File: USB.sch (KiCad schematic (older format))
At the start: 41 parts, among them J6 USB_A, J7 USB_B, U10 USB3320, U11 MIC2025-1YMM, U12 USB3320, U20 xc7z020clg484, Y1 ABM3-24.000MHZ-D2Y-T, Y2 ABM3-24.000MHZ-D2Y-T

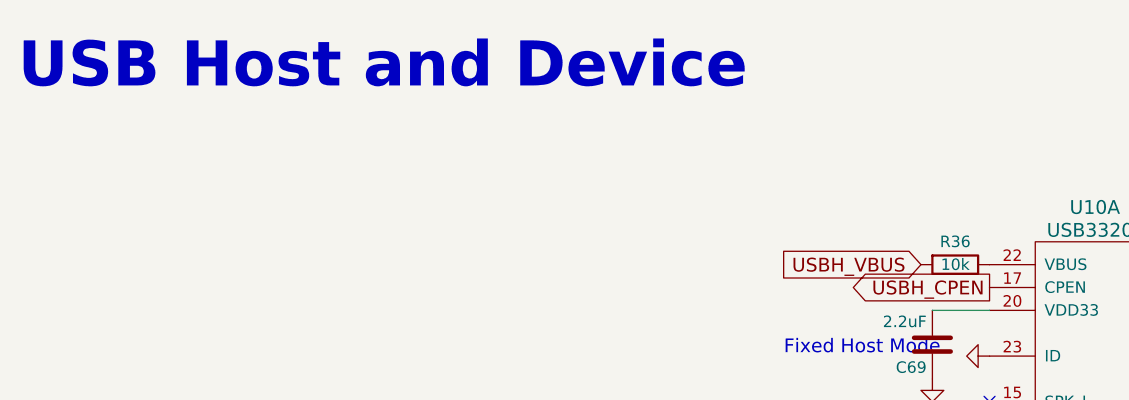
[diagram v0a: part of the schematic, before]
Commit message: low 2 ddr3 bytes delay matched WRT package flight time
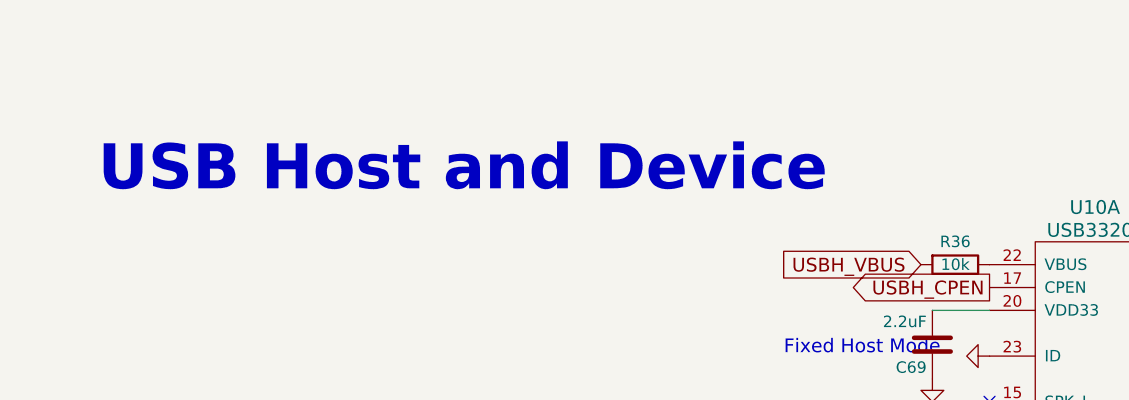
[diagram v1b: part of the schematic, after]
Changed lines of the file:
@@
 	1    0    0    -1
 $EndComp
-Text Notes 250  550  0    197  ~ 39
+Text Notes 600  1000 0    197  ~ 39
 USB Host and Device
 $EndSCHEMATC

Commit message: added arduino header, shifted components, deleted 50pin ZIF, deleted MIDI in for fear of confusion with headphone jack
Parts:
- J7: footprint Connector_USB:USB_B_Amphenol_MUSB-D511_Vertical_Rugged -> Connector_USB:USB_B_OST_USB-B1HSxx_Horizontal
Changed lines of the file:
@@
 F 0 "J7" H 9305 5367 50  0000 C CNN
 F 1 "USB_B" H 9305 5276 50  0000 C CNN
-F 2 "Connector_USB:USB_B_Amphenol_MUSB-D511_Vertical_Rugged" H 9400 4850 50  0001 C CNN
+F 2 "Connector_USB:USB_B_OST_USB-B1HSxx_Horizontal" H 9400 4850 50  0001 C CNN
 F 3 " ~" H 9400 4850 50  0001 C CNN
 	1    9250 4900

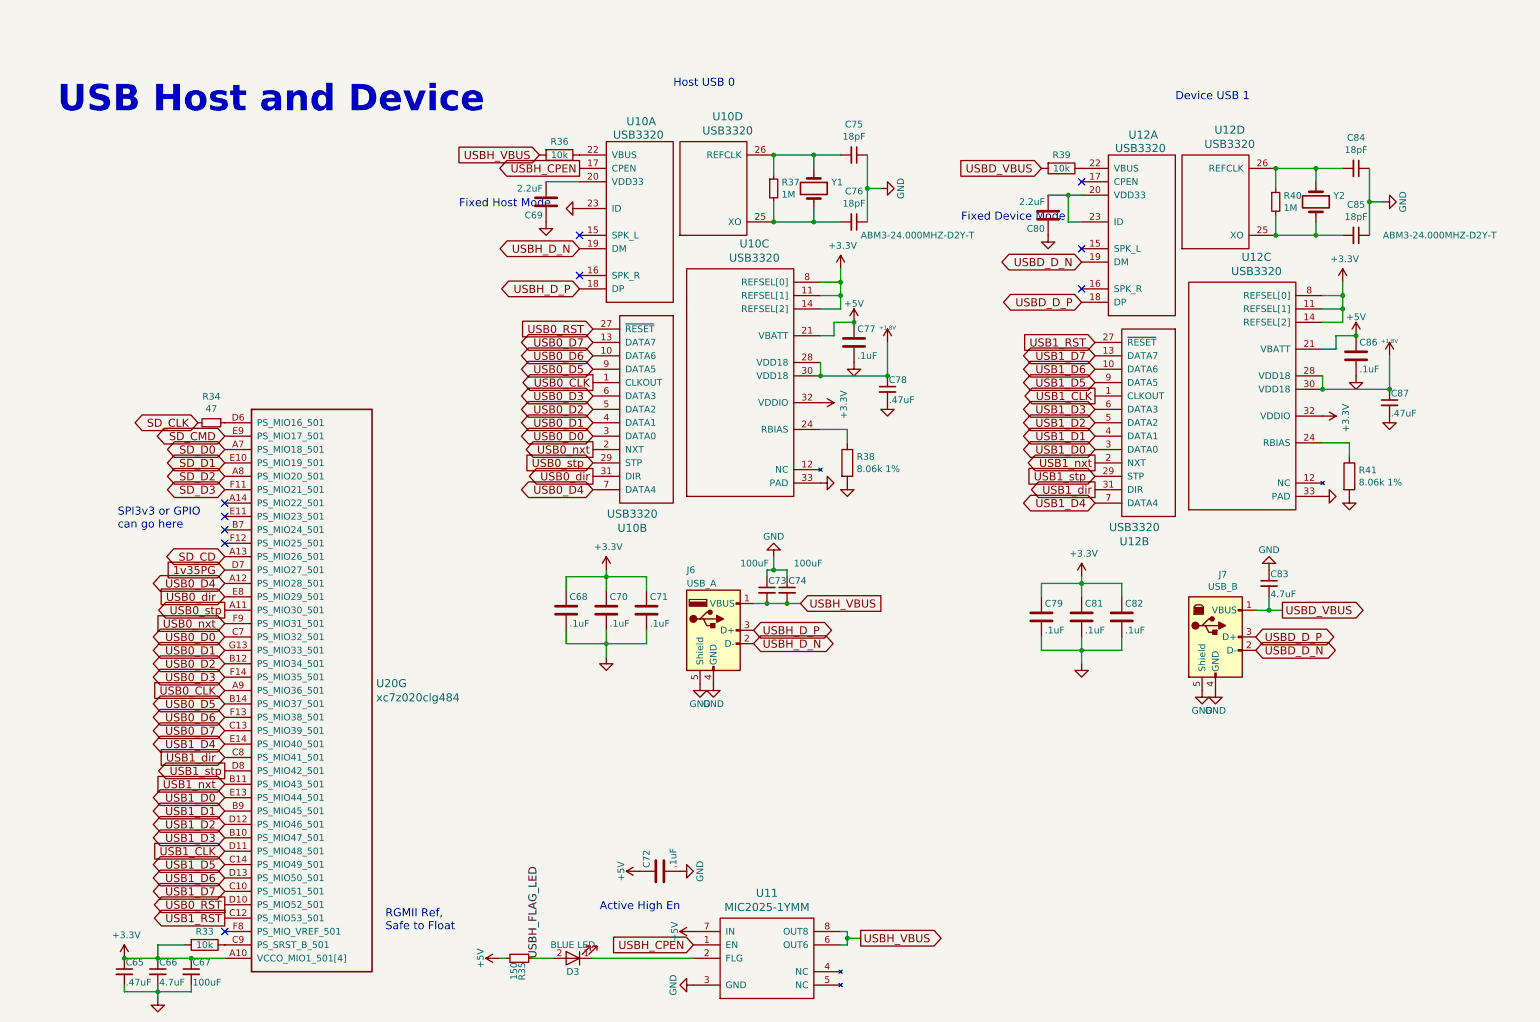
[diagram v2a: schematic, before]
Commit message: downto 70 unrouted. moved SD interface back to MIO
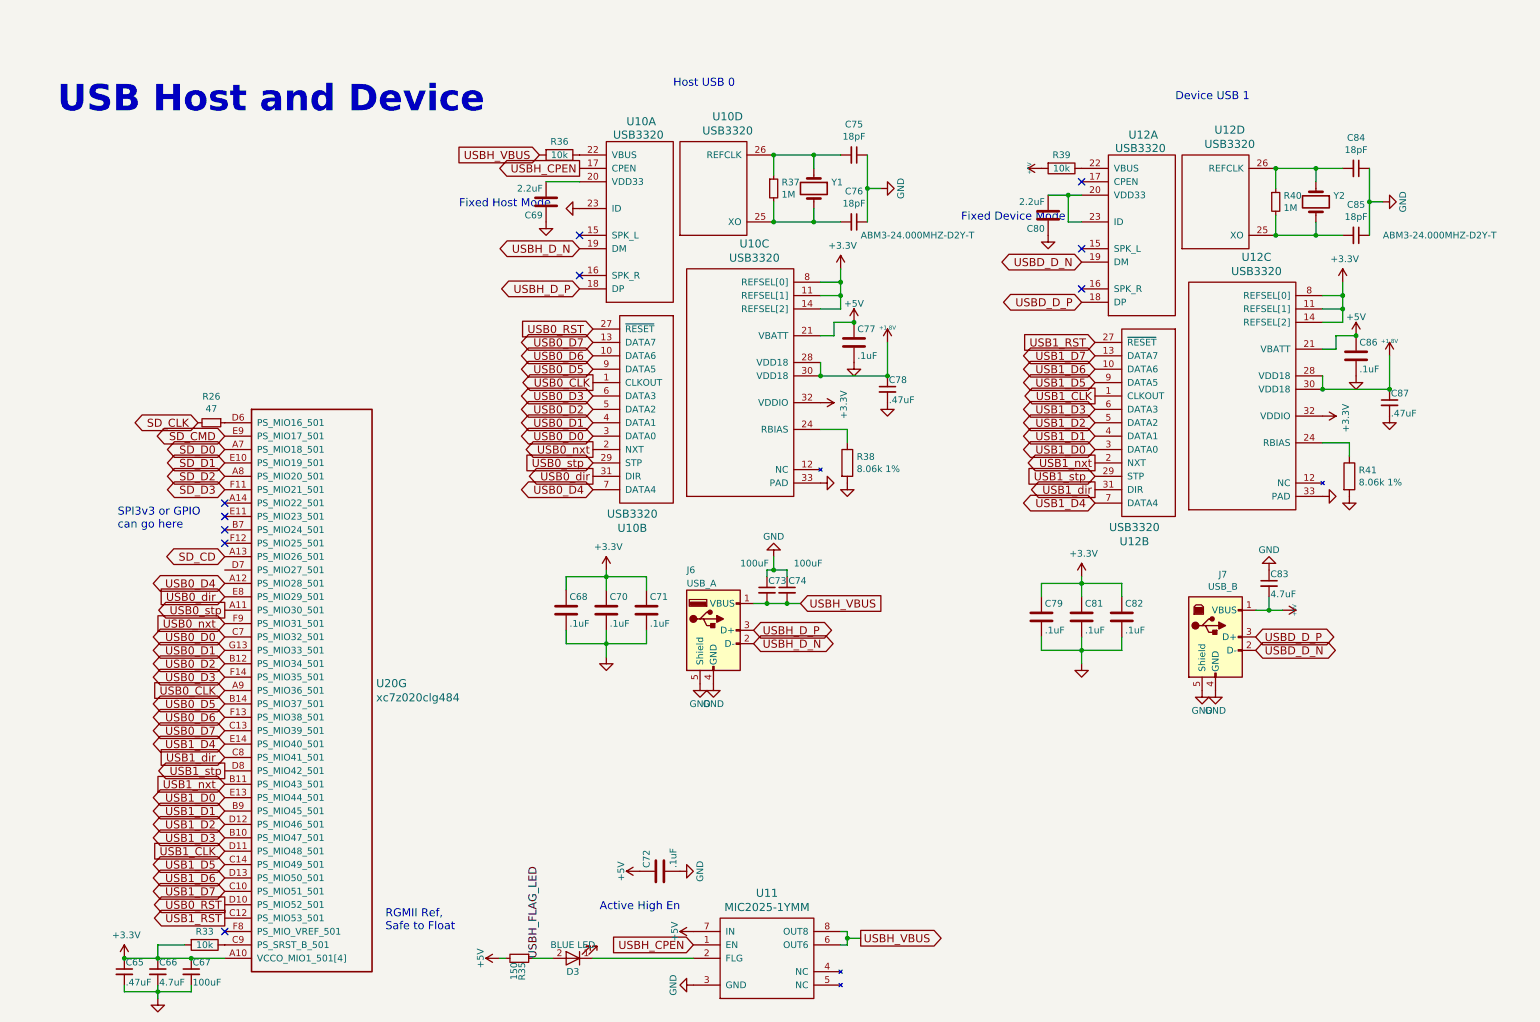
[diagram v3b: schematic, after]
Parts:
- removed R34: 47, Resistor_SMD:R_0402_1005Metric, symbol Device:R_Small
- added R26: 47, Resistor_SMD:R_0402_1005Metric, symbol Device:R_Small
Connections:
- net USBD_VBUS is gone; now on net +5V: C83.2, J7.1 (VBUS), R39.2
- net SD_CLK: now also R26.2
- net at U20.D6 (PS_MIO16_501): now also R26.1
- net 1v35PG: no longer names the net of U20.D7 (PS_MIO27_501)
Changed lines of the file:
@@
 Comment4 ""
 $EndDescr
-Text GLabel 1850 3500 0    60   BiDi ~ 0
-SD_D0
-Text GLabel 1850 3600 0    60   BiDi ~ 0
-SD_D1
-Text GLabel 1850 3700 0    60   BiDi ~ 0
-SD_D2
-Text GLabel 1850 3800 0    60   BiDi ~ 0
-SD_D3
-Text GLabel 1850 3400 0    60   BiDi ~ 0
-SD_CMD
-Text GLabel 1650 3300 0    60   BiDi ~ 0
-SD_CLK
-Text GLabel 1850 4300 0    60   BiDi ~ 0
-SD_CD
 $Comp
 L power:+5V #PWR0110
@@
 	0    1    1    0
 $EndComp
-Text GLabel 7950 1400 0    60   Input ~ 0
-USBD_VBUS
 NoConn ~ 8250 2000
 NoConn ~ 8250 2300
@@
 	9700 1750 9700 1900
 Connection ~ 9700 1900
-Text GLabel 9750 4700 2    60   Output ~ 0
-USBD_VBUS
 Text GLabel 9550 5000 2    60   BiDi ~ 0
 USBD_D_N
@@
 	8150 1600 8000 1600
 NoConn ~ 1850 7100
-$Comp
-L Device:R_Small R34
-U 1 1 5CAB588F
-P 1750 3300
-F 0 "R34" V 1554 3300 50  0000 C CNN
-F 1 "47" V 1645 3300 50  0000 C CNN
-F 2 "Resistor_SMD:R_0402_1005Metric" H 1750 3300 50  0001 C CNN
-F 3 "~" H 1750 3300 50  0001 C CNN
-	1    1750 3300
-	0    1    1    0
-$EndComp
 $Comp
 L Device:R R?
@@
 Text Notes 1050 4100 0    60   ~ 0
 SPI3v3 or GPIO \ncan go here\n
-Text GLabel 1850 4400 0    60   Input ~ 0
-1v35PG
 $Comp
 L power:+3V3 #PWR0101
@@
 Text Notes 600  1000 0    197  ~ 39
 USB Host and Device
+$Comp
+L power:+5V #PWR?
+U 1 1 5DE2EB64
+P 7950 1400
+AR Path="/58508414/5DE2EB64" Ref="#PWR?"  Part="1"
+AR Path="/5852A88E/5DE2EB64" Ref="#PWR0180"  Part="1"
+F 0 "#PWR0180" H 7950 1490 20  0001 C CNN
+F 1 "+5V" H 7950 1490 30  0000 C CNN
+F 2 "" H 7950 1400 60  0001 C CNN
+F 3 "" H 7950 1400 60  0001 C CNN
+	1    7950 1400
+	0    -1   -1   0
+$EndComp
+$Comp
+L power:+5V #PWR0181
+U 1 1 5DE3808F
+P 9750 4700
+F 0 "#PWR0181" H 9750 4790 20  0001 C CNN
+F 1 "+5V" H 9750 4790 30  0000 C CNN
+F 2 "" H 9750 4700 60  0001 C CNN
+F 3 "" H 9750 4700 60  0001 C CNN
+	1    9750 4700
+	0    1    1    0
+$EndComp
+Text GLabel 1650 3300 0    60   BiDi ~ 0
+SD_CLK
+$Comp
+L Device:R_Small R26
+U 1 1 5DD165E9
+P 1750 3300
+AR Path="/5852A88E/5DD165E9" Ref="R26"  Part="1"
+AR Path="/58508444/5DD165E9" Ref="R?"  Part="1"
+F 0 "R26" V 1554 3300 50  0000 C CNN
+F 1 "47" V 1645 3300 50  0000 C CNN
+F 2 "Resistor_SMD:R_0402_1005Metric" H 1750 3300 50  0001 C CNN
+F 3 "~" H 1750 3300 50  0001 C CNN
+	1    1750 3300
+	0    1    1    0
+$EndComp
+Text GLabel 1850 3700 0    60   BiDi ~ 0
+SD_D2
+Text GLabel 1850 3500 0    60   BiDi ~ 0
+SD_D0
+Text GLabel 1850 3600 0    60   BiDi ~ 0
+SD_D1
+Text GLabel 1850 3400 0    60   BiDi ~ 0
+SD_CMD
+Text GLabel 1850 3800 0    60   BiDi ~ 0
+SD_D3
+Text GLabel 1850 4300 0    60   BiDi ~ 0
+SD_CD
 $EndSCHEMATC

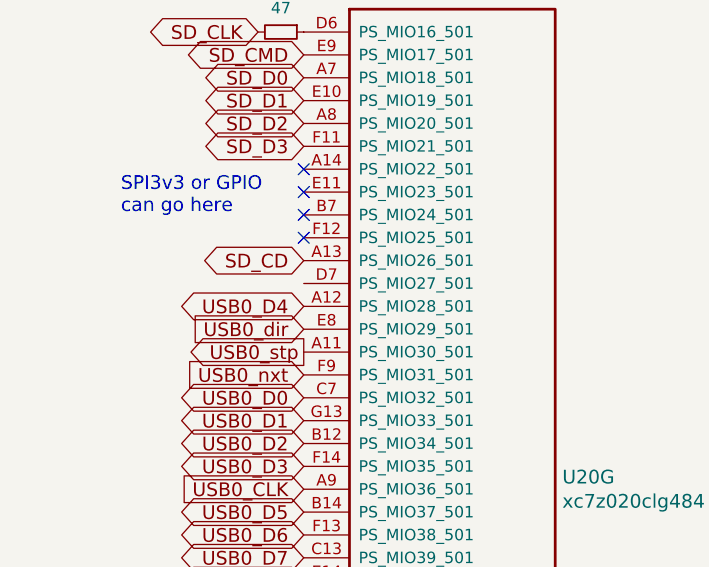
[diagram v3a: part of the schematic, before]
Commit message: DRC passes with only GNDTIE errors. no unconnected. power plane quality unknown
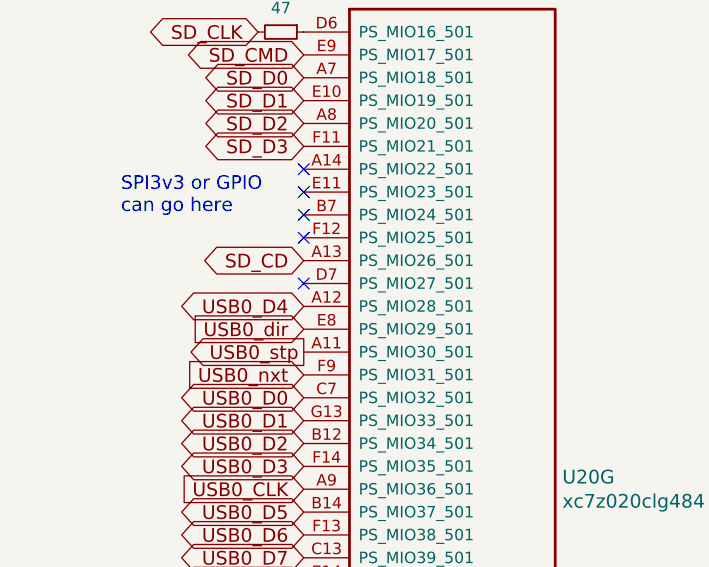
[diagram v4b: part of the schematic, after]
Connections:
- no-connect marks 10 -> 11
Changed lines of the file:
@@
 Text GLabel 1850 4300 0    60   BiDi ~ 0
 SD_CD
+NoConn ~ 1850 4400
 $EndSCHEMATC

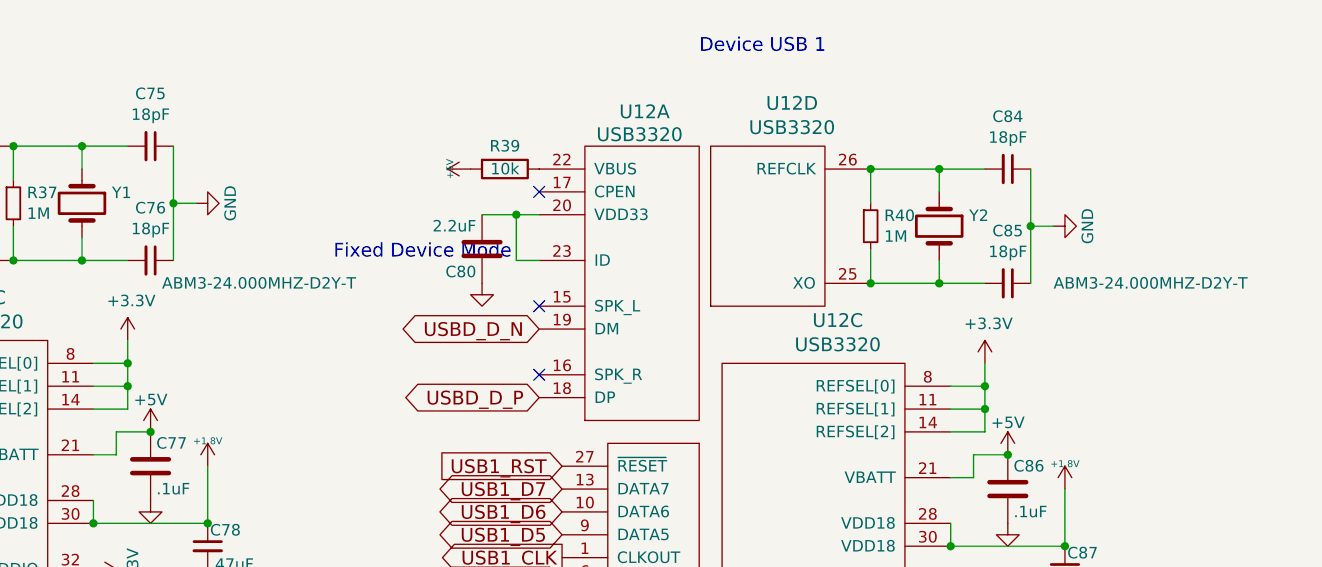
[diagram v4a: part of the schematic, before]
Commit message: length matched important interfaces, added current sense resistors to regulators, about to shrink silkscreen designators
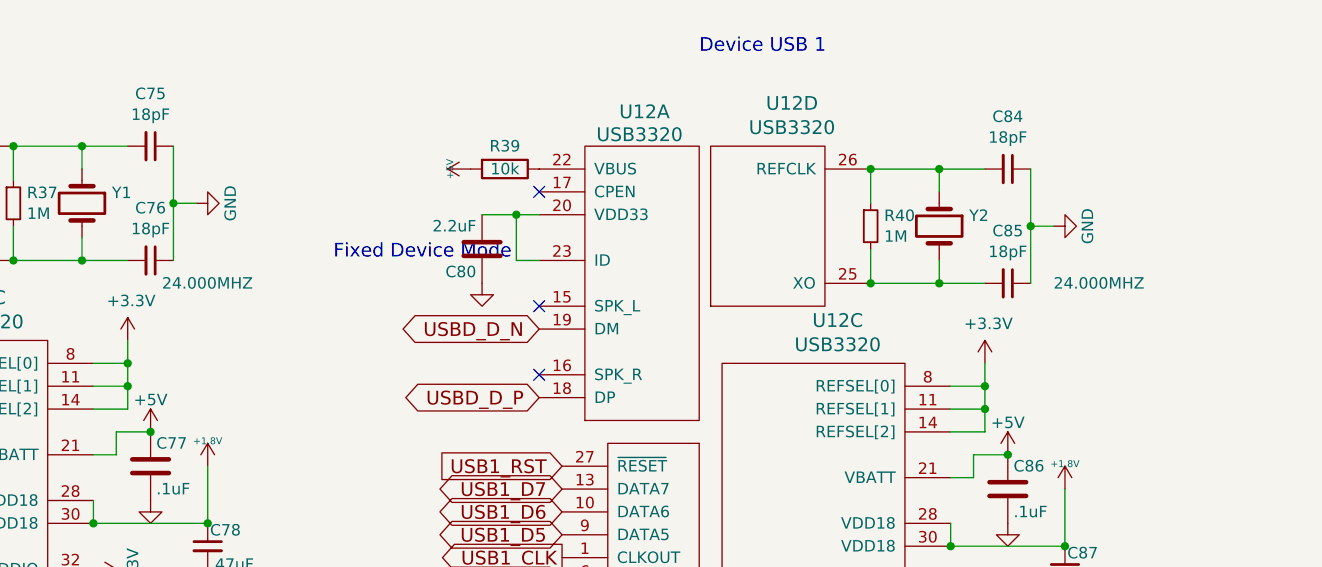
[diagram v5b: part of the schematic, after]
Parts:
- C75, C76, C84, C85: MFR (none) -> Murata; MPN (none) -> GCM1555C1H180JA16D; SPN (none) -> 490-12650-1-ND; SPR (none) -> Digikey; SPURL (none) -> -
- J6: MFR (none) -> Amphenol ICC; MPN (none) -> 87583-2010RLF; SPN (none) -> 609-5390-1-ND; SPR (none) -> Digikey; SPURL (none) -> -
- J7: MFR (none) -> On Shore Technology; MPN (none) -> USB-B1HSW6; SPN (none) -> ED2982-ND; SPR (none) -> Digikey; SPURL (none) -> -
- R26: MFR (none) -> Yageo; MPN (none) -> RC0402JR-0747RL; SPN (none) -> 311-47JRTR-ND; SPR (none) -> Digikey; SPURL (none) -> -
- R37, R40: MFR (none) -> Yageo; MPN (none) -> RC0402FR-071ML; SPN (none) -> 311-1.00MLRCT-ND; SPR (none) -> Digikey; SPURL (none) -> -
- R38, R41: MFR (none) -> Yageo; MPN (none) -> RC0402FR-078K06L; SPN (none) -> 311-8.06KLRTR-ND; SPR (none) -> Digikey; SPURL (none) -> -
- U10, U12: MFR (none) -> Microchip Technology; MPN (none) -> USB3320C-EZK-TR; SPN (none) -> USB3320C-EZK-CT-NDs; SPR (none) -> Digikey; SPURL (none) -> -
- U11: MFR (none) -> Microchip; MPN (none) -> MIC2025-1YMM-TR; SPN (none) -> MIC2025-1YMM-CT-ND; SPR (none) -> Digikey; SPURL (none) -> -
- U20: MFR (none) -> Xilinx; MPN (none) -> XC7Z020-1CLG484C; SPN (none) -> 122-1850-ND; SPR (none) -> Digikey; SPURL (none) -> -
- Y1, Y2: value ABM3-24.000MHZ-D2Y-T -> 24.000MHZ; MFR (none) -> Abracon LLC; MPN (none) -> ABM3-24.000MHZ-D2Y-T; SPN (none) -> 535-10643-2-ND; SPR (none) -> DigiKey; SPURL (none) -> -
